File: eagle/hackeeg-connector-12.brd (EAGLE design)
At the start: 77.7 x 27.9 mm, 13 parts

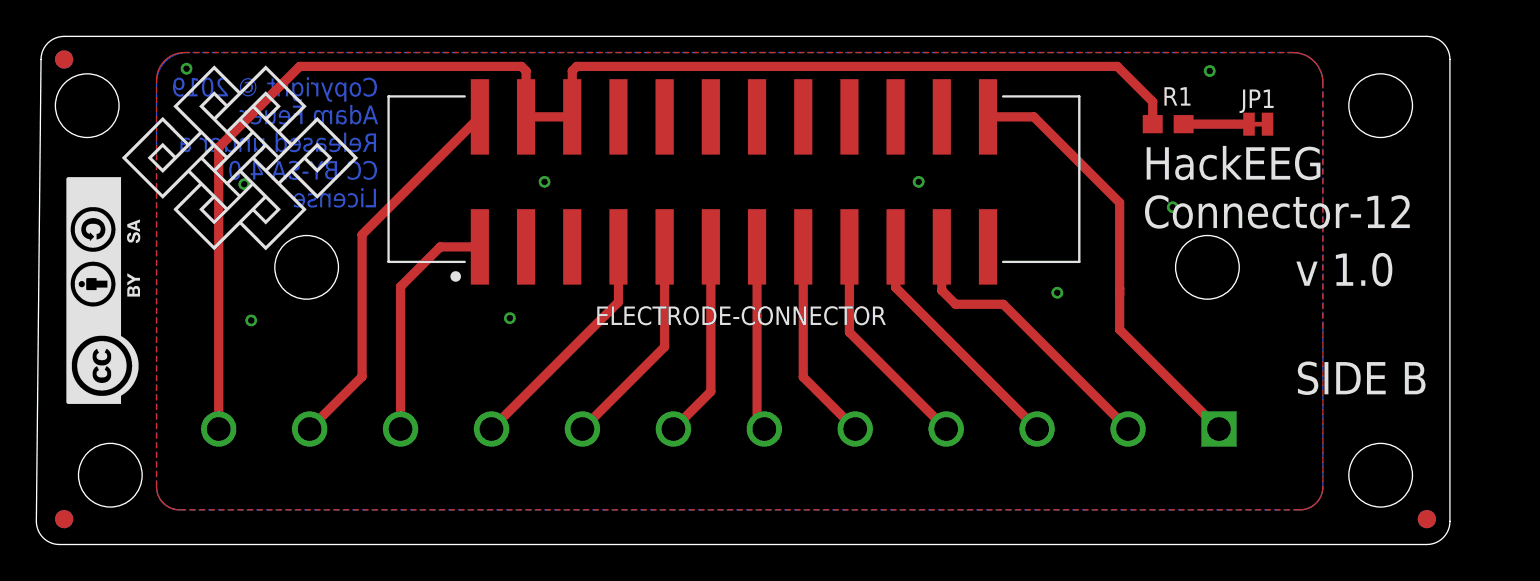
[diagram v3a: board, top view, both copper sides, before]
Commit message: relicense to CERN OHL 1.2 - sch and brd
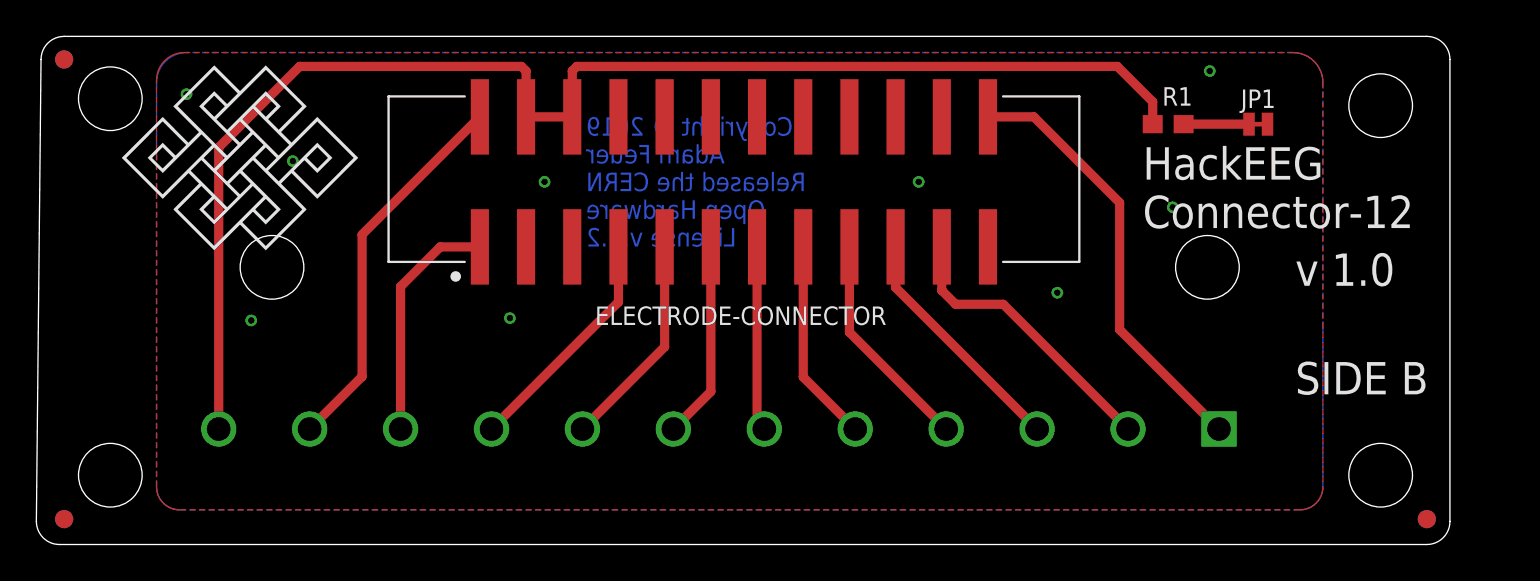
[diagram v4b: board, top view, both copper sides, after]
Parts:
- removed FRAME1: FRAME-LETTER, SparkFun-Aesthetics:CREATIVE_COMMONS
- removed U$13: CC-BY-SA, creative-commons:CC-BY-SA
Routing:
- net DVDD: track 14.8 -> 13.1 mm
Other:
- board text added: "Copyright © 2019 Adam Feuer Released the CERN Open Hardware License v.1.2"
- board text removed: "Copyright © 2019 Adam Feuer Released under a CC BY-SA 4.0 License"
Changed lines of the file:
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@@
 <board>
 <plain>
-<text x="37.592" y="21.082" size="1.016" layer="16" rot="MR0">Copyright © 2019
+<text x="49.022" y="26.035" size="1.016" layer="16" font="vector" ratio="13" rot="MR180">Copyright © 2019
 Adam Feuer
-Released under a
-CC BY-SA 4.0
-License</text>
-<hole x="21.59" y="26.67" drill="3.49999375"/>
+Released the CERN
+Open Hardware
+License v.1.2</text>
+<hole x="22.86" y="27.051" drill="3.49999375"/>
 <hole x="22.86" y="6.35" drill="3.49999375"/>
 <hole x="92.71" y="6.35" drill="3.49999375"/>
@@
 <text x="95.377" y="8.509" size="1.778" layer="26" rot="MR0">SIDE A</text>
 <text x="88.011" y="10.795" size="1.778" layer="25">SIDE B</text>
-<hole x="33.655" y="17.78" drill="3.49999375"/>
+<hole x="31.75" y="17.78" drill="3.49999375"/>
 <hole x="83.185" y="17.78" drill="3.49999375"/>
 <dimension x1="-2.54" y1="30.48" x2="-2.54" y2="2.54" x3="-8.89" y3="16.51" textsize="1.778" layer="47" unit="inch"/>
@@
 <attribute name="VALUE" x="38.0449" y="14.83696875" size="1.78313125" layer="27"/>
 </element>
-<element name="FRAME1" library="SparkFun-Aesthetics" library_urn="urn:adsk.eagle:library:507" package="CREATIVE_COMMONS" package3d_urn="urn:adsk.eagle:package:37121/1" value="FRAME-LETTER" x="24.13" y="-10.16" smashed="yes"/>
 <element name="U$1" library="endless-knot" package="ENDLESSKNOT-MEDIUM" value="ENDLESSKNOTENDLESSKNOT-MEDIUM" x="30.099" y="23.749" smashed="yes"/>
-<element name="U$13" library="creative-commons" package="CC-BY-SA" value="CC-BY-SA" x="24.765" y="10.16" smashed="yes" rot="R90"/>
 <element name="FD1" library="SparkFun-Aesthetics" library_urn="urn:adsk.eagle:library:507" package="FIDUCIAL-1X2" package3d_urn="urn:adsk.eagle:package:37108/1" value="FIDUCIAL1X2" x="20.32" y="3.937" smashed="yes"/>
 <element name="FD2" library="SparkFun-Aesthetics" library_urn="urn:adsk.eagle:library:507" package="FIDUCIAL-1X2" package3d_urn="urn:adsk.eagle:package:37108/1" value="FIDUCIAL1X2" x="20.32" y="29.21" smashed="yes"/>
@@
 <vertex x="25.4" y="27.94"/>
 </polygon>
-<via x="27.051" y="28.702" extent="1-16" drill="0.35"/>
-<via x="30.226" y="22.352" extent="1-16" drill="0.35"/>
+<via x="27.051" y="27.305" extent="1-16" drill="0.35"/>
+<via x="32.893" y="23.622" extent="1-16" drill="0.35"/>
 <via x="46.736" y="22.479" extent="1-16" drill="0.35"/>
 <via x="67.31" y="22.479" extent="1-16" drill="0.35"/>
@@
 <signal name="DVDD">
 <contactref element="ELECTRODE-CONNECTOR" pad="1"/>
-<wire x1="43.18" y1="18.904" x2="43.034" y2="19.05" width="0.508" layer="1"/>
-<wire x1="43.18" y1="18.904" x2="43.18" y2="19.05" width="0.508" layer="1"/>
-<wire x1="43.18" y1="19.05" x2="43.18" y2="20.447" width="0.508" layer="1"/>
 <contactref element="WIRE-CONNECTOR" pad="10"/>
 <wire x1="43.18" y1="18.904" x2="41.002" y2="18.904" width="0.508" layer="1"/>
@@
 <contactref element="WIRE-CONNECTOR" pad="1"/>
 <wire x1="71.12" y1="26.054" x2="73.641" y2="26.054" width="0.508" layer="1"/>
-<wire x1="78.359" y1="21.336" x2="78.359" y2="16.637" width="0.508" layer="1"/>
-<wire x1="78.359" y1="16.637" x2="78.359" y2="16.256" width="0.508" layer="1"/>
 <wire x1="73.641" y1="26.054" x2="78.359" y2="21.336" width="0.508" layer="1"/>
-<wire x1="83.82" y1="8.89" x2="78.359" y2="14.351" width="0.508" layer="1"/>
-<wire x1="78.359" y1="14.351" x2="78.359" y2="16.637" width="0.508" layer="1"/>
+<wire x1="78.359" y1="14.351" x2="83.82" y2="8.89" width="0.508" layer="1"/>
+<wire x1="78.359" y1="21.336" x2="78.359" y2="14.351" width="0.508" layer="1"/>
 </signal>
 </signals>
